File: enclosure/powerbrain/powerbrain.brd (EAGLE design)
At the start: 24.8 x 64.8 mm, 41 parts, among them Q2 200mA/50V, X2 ZX62D-B-5PA8

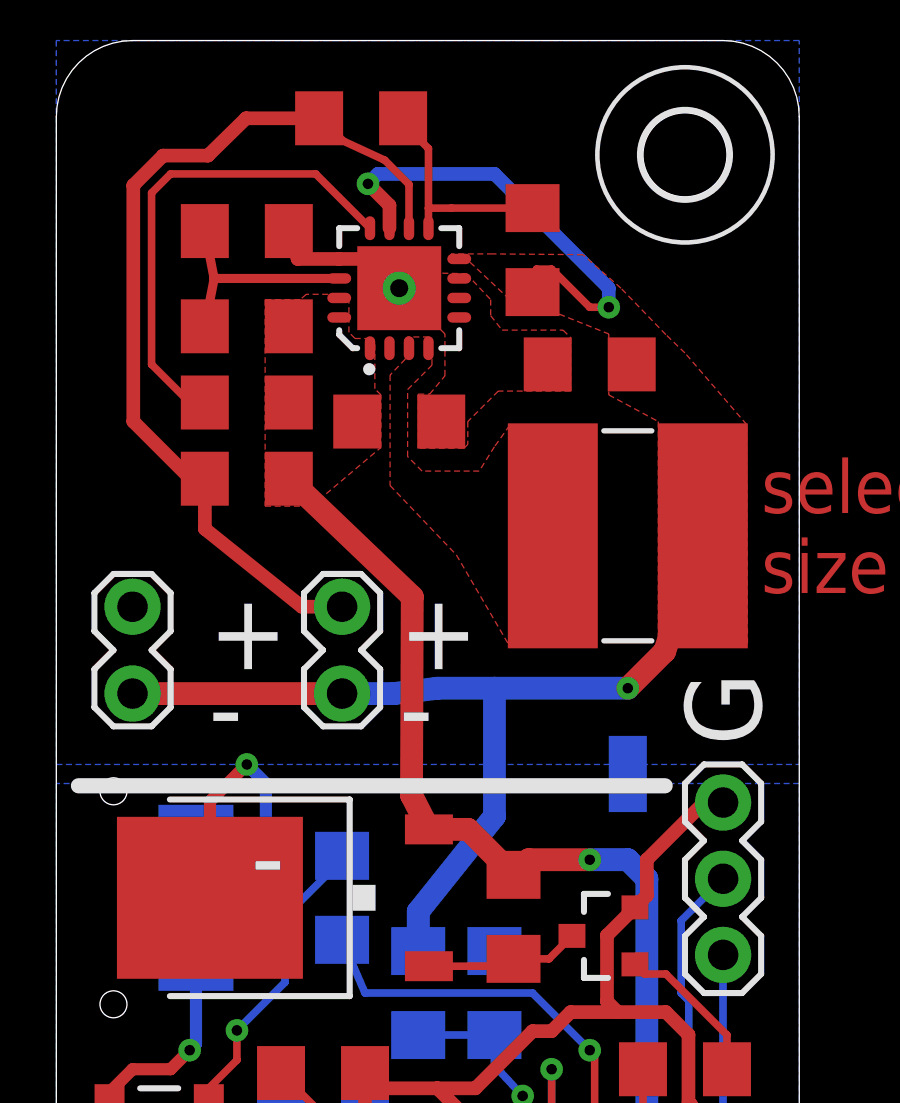
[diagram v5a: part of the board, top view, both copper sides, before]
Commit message: powerbrain: traces cleaned up
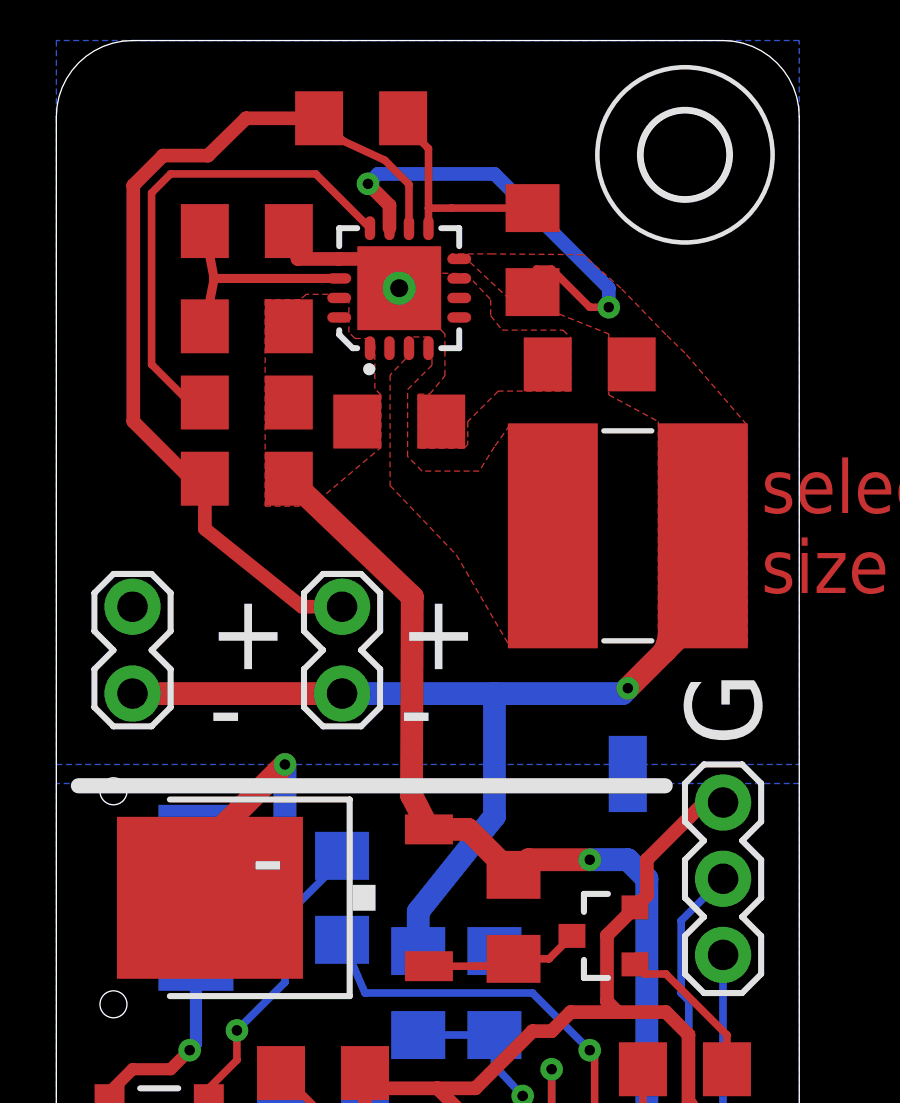
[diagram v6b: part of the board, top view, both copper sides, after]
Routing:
- net BATT_VCC: track 47.9 -> 49.6 mm
- net USB_VCC: track 11.6 -> 12.1 mm
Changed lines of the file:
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@@
 <vertex x="20.066" y="44.6786"/>
 </polygon>
-<wire x1="10.1854" y1="59.9948" x2="10.16" y2="59.9948" width="0.254" layer="1"/>
 <via x="10.3886" y="59.9948" extent="1-16" drill="0.35"/>
 <wire x1="12.065" y1="34.42" x2="12.065" y2="35.7378" width="0.762" layer="16"/>
-<wire x1="14.605" y1="38.9128" x2="12.065" y2="35.7378" width="0.762" layer="16"/>
+<wire x1="12.065" y1="35.7378" x2="14.605" y2="38.9128" width="0.762" layer="16"/>
 <via x="18.415" y="55.88" extent="1-16" drill="0.35"/>
 <wire x1="17.78" y1="55.88" x2="18.415" y2="55.88" width="0.254" layer="1"/>
@@
 <wire x1="16.51" y1="57.15" x2="16.005" y2="57.15" width="0.254" layer="1"/>
 <wire x1="16.005" y1="57.15" x2="15.875" y2="56.385" width="0.254" layer="1"/>
-<wire x1="9.525" y1="43.0022" x2="11.2522" y2="43.0022" width="0.762" layer="16"/>
-<wire x1="11.2522" y1="43.0022" x2="12.7" y2="43.18" width="0.762" layer="16"/>
-<wire x1="12.7" y1="43.18" x2="14.605" y2="43.18" width="0.762" layer="16"/>
-<wire x1="14.605" y1="43.18" x2="14.605" y2="38.9128" width="0.762" layer="16"/>
-<wire x1="14.605" y1="43.18" x2="19.05" y2="43.18" width="0.762" layer="16"/>
-<via x="19.05" y="43.18" extent="1-16" drill="0.35"/>
 <wire x1="21.55" y1="48.26" x2="20.28" y2="44.41" width="0.762" layer="1"/>
-<wire x1="20.28" y1="44.41" x2="19.05" y2="43.18" width="0.762" layer="1"/>
 <contactref element="J4" pad="2"/>
 <wire x1="2.54" y1="43.0022" x2="9.525" y2="43.0022" width="0.762" layer="1"/>
@@
 <wire x1="14.605" y1="60.325" x2="10.7188" y2="60.325" width="0.4572" layer="16"/>
 <wire x1="10.7188" y1="60.325" x2="10.3886" y2="59.9948" width="0.4572" layer="16"/>
-<wire x1="10.3886" y1="59.9948" x2="10.1854" y2="59.9948" width="0" layer="19" extent="1-1"/>
+<wire x1="14.605" y1="43.0022" x2="9.525" y2="43.0022" width="0.762" layer="16"/>
+<wire x1="14.605" y1="43.0022" x2="18.8722" y2="43.0022" width="0.762" layer="16"/>
+<wire x1="18.8722" y1="43.0022" x2="19.05" y2="43.18" width="0.762" layer="16"/>
+<via x="19.05" y="43.18" extent="1-16" drill="0.35"/>
+<wire x1="19.05" y1="43.18" x2="21.59" y2="45.72" width="0.762" layer="1"/>
+<wire x1="14.605" y1="38.9128" x2="14.605" y2="43.0022" width="0.762" layer="16"/>
 </signal>
 <signal name="N$4">
@@
 <signal name="USB_VCC">
 <contactref element="Q1" pad="3"/>
-<wire x1="5.12" y1="36.195" x2="5.12" y2="39.41" width="0.4064" layer="1"/>
-<wire x1="5.12" y1="39.41" x2="6.35" y2="40.64" width="0.4064" layer="1"/>
-<via x="6.35" y="40.64" extent="1-16" drill="0.35"/>
 <contactref element="S2" pad="2"/>
-<wire x1="4.655" y1="36.195" x2="6.35" y2="36.195" width="0.4064" layer="16"/>
-<wire x1="6.35" y1="36.195" x2="6.985" y2="36.83" width="0.4064" layer="16"/>
-<wire x1="6.985" y1="36.83" x2="6.985" y2="40.005" width="0.4064" layer="16"/>
-<wire x1="6.985" y1="40.005" x2="6.35" y2="40.64" width="0.4064" layer="16"/>
+<wire x1="5.12" y1="36.195" x2="5.12" y2="38.14" width="0.762" layer="1"/>
+<wire x1="5.12" y1="38.14" x2="7.62" y2="40.64" width="0.762" layer="1"/>
+<via x="7.62" y="40.64" extent="1-16" drill="0.35"/>
+<wire x1="7.62" y1="40.64" x2="7.62" y2="37.465" width="0.762" layer="16"/>
+<wire x1="7.62" y1="37.465" x2="6.35" y2="36.195" width="0.762" layer="16"/>
+<wire x1="6.35" y1="36.195" x2="4.655" y2="36.195" width="0.762" layer="16"/>
 </signal>
 <signal name="FOO3">

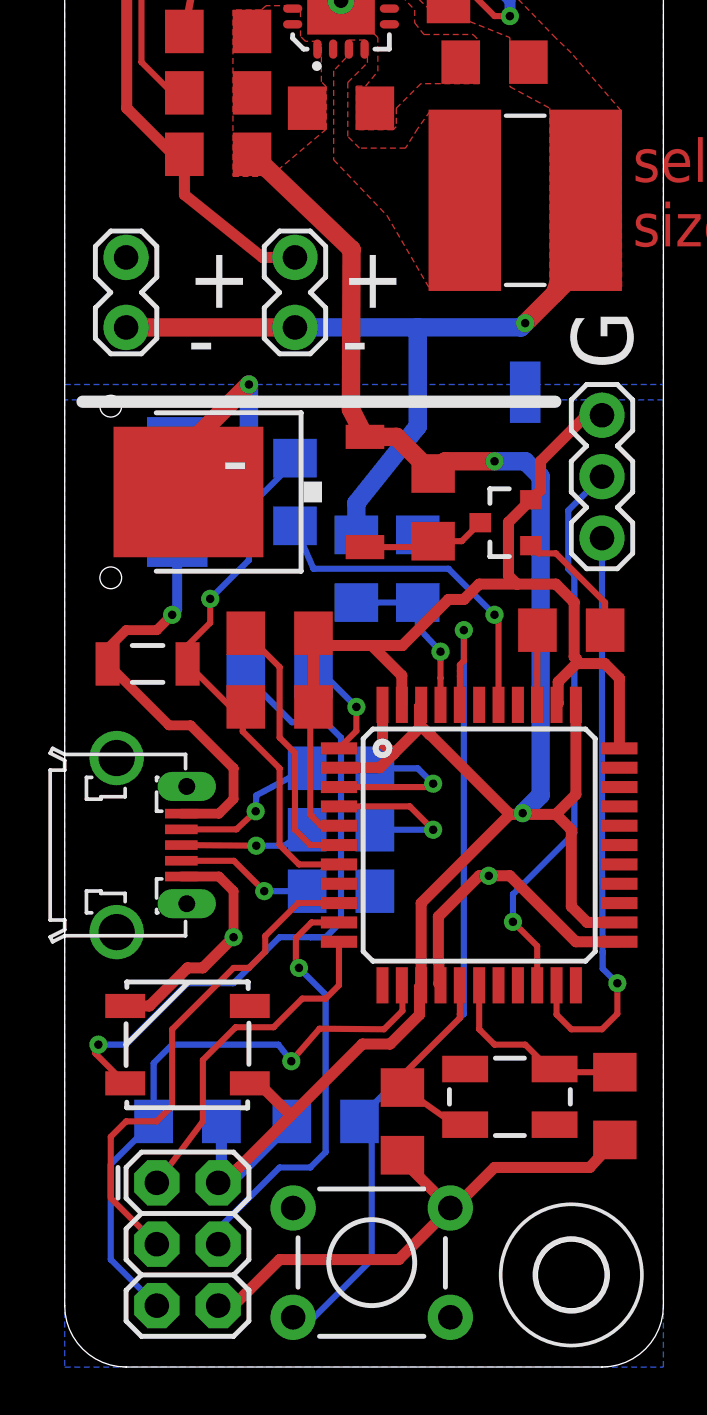
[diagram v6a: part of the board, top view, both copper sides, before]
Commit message: powerbrain: decoupling capacitor for battery voltage divider
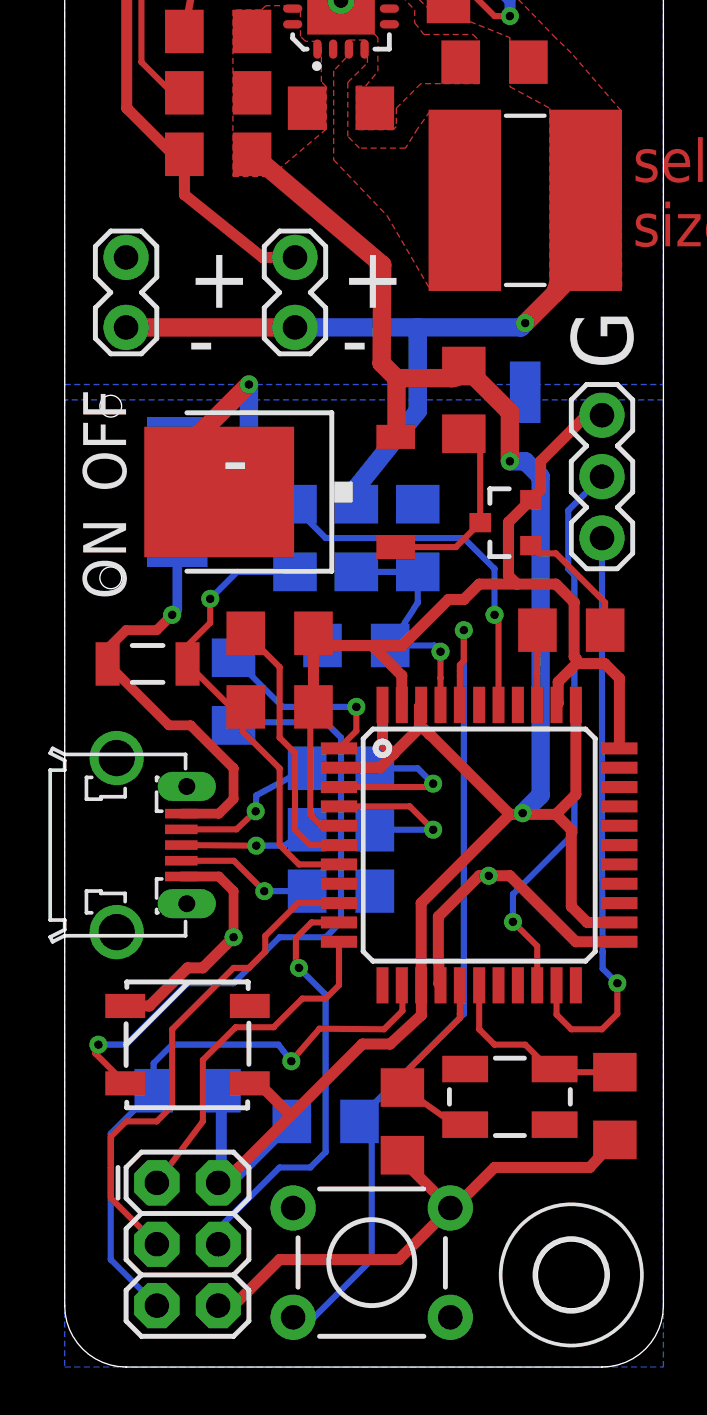
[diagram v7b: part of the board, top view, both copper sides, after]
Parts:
- added C1: 0.1uF, SparkFun-Passives:1206
- moved R3 4.62 mm to (16.5, 40.0)
- moved R_LED 2.01 mm to (6.99, 27.9), turned to 270 degrees
- moved RUSB3 1.91 mm to (9.53, 34.3), turned to 90 degrees
- moved Q1 1.27 mm to (8.89, 36.2)
- moved RRST 1.27 mm to (5.08, 11.4)
- moved VD1 1.27 mm to (12.1, 34.3)
- moved VD2 1.27 mm to (14.6, 34.3)
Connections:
- net GND: now also C1.2
- net VD_DIRECT: now also C1.1
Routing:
- net LED: track 4.31 -> 7.94 mm
- net $N23: track 22.7 -> 19.4 mm
- net VD_DIRECT: track 7.14 -> 10.3 mm
- net VCC: track 91.8 -> 94.9 mm
- net N$6: track 5.19 -> 7.88 mm
- net BATT_VCC: track 49.6 -> 48.3 mm
- net VBUS_SENSE: track 14.0 -> 15.1 mm
- net N$7: track 27.6 -> 26.7 mm
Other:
- board text added: "OFF"
- board text added: "ON"

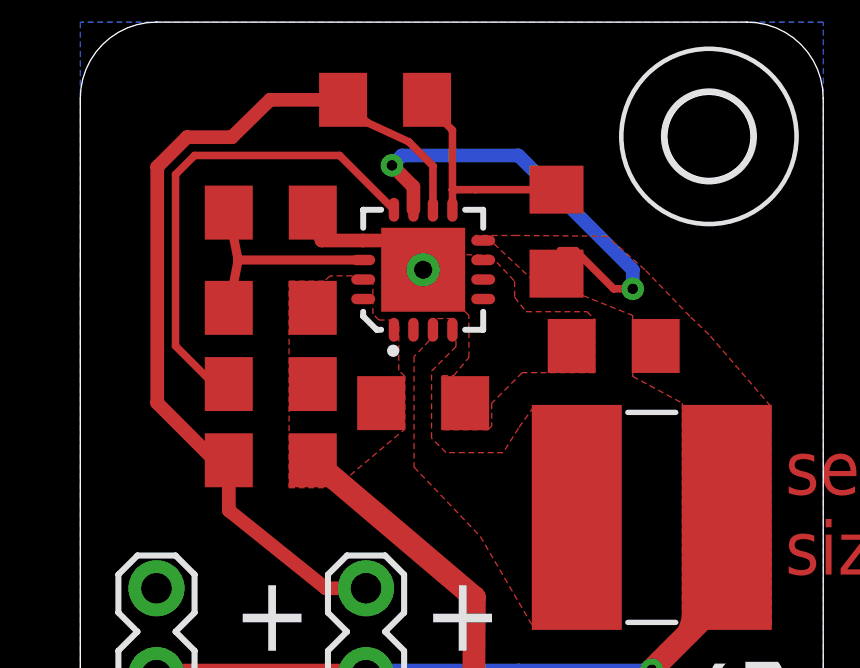
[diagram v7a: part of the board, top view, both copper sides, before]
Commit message: powerbrain: low battery output
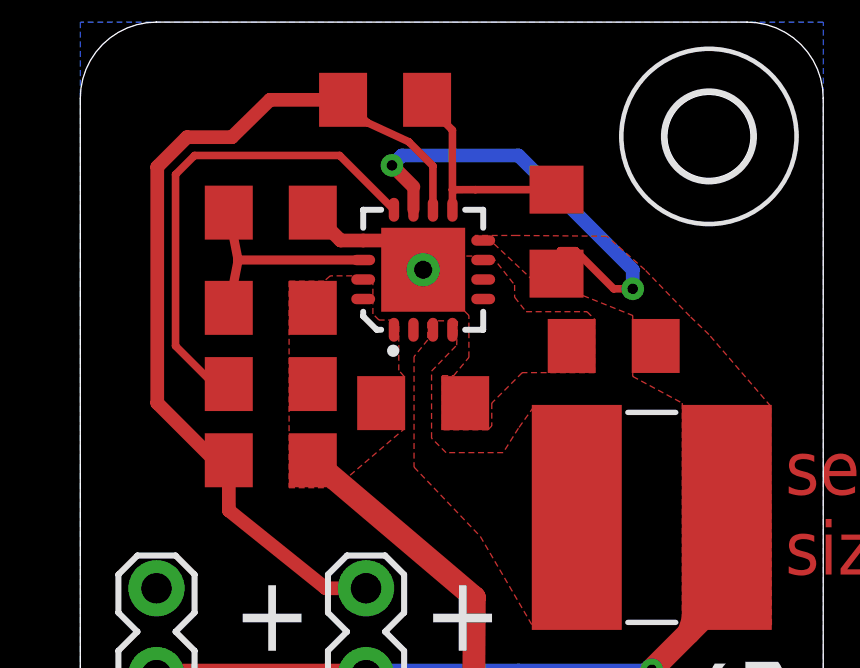
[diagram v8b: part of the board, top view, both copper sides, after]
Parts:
- BL1: value (none) -> 6.8uH / 2A
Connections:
- net N$16 renamed LOW_BATTERY_OUTPUT
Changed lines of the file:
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@@
 <?xml version="1.0" encoding="utf-8"?>
 <!DOCTYPE eagle SYSTEM "eagle.dtd">
-<eagle version="8.2.1">
+<eagle version="8.2.2">
 <drawing>
 <settings>
@@
 <attribute name="VALUE" x="6.35" y="46.99" size="1.27" layer="27" rot="R270"/>
 </element>
-<element name="BL1" library="SparkFun-Passives" package="NPI75C" value="" x="19.05" y="48.26" smashed="yes"/>
+<element name="BL1" library="SparkFun-Passives" package="NPI75C" value="6.8uH / 2A" x="19.05" y="48.26" smashed="yes"/>
 <element name="R3" library="SparkFun-Resistors" package="1206" value="10k" x="16.51" y="40.005" smashed="yes" rot="R270"/>
 <element name="R7" library="SparkFun-Resistors" package="1206" value="1k" x="20.955" y="30.48" smashed="yes"/>
@@
 <wire x1="13.208" y1="27.327" x2="13.145" y2="27.39" width="0.254" layer="1"/>
 <polygon width="0.0254" layer="1" thermals="no">
-<vertex x="10.8204" y="51.2064"/>
-<vertex x="10.8204" y="52.959"/>
+<vertex x="10.795" y="51.2064"/>
+<vertex x="10.795" y="52.959"/>
 <vertex x="10.6172" y="53.1622"/>
 <vertex x="10.6172" y="54.6862"/>
@@
 <contactref element="J4" pad="2"/>
 <wire x1="2.54" y1="43.0022" x2="9.525" y2="43.0022" width="0.762" layer="1"/>
-<wire x1="11.105" y1="58.515" x2="11.105" y2="59.2784" width="0.4572" layer="1"/>
+<wire x1="11.105" y1="58.515" x2="11.105" y2="59.2784" width="0.4064" layer="1"/>
 <wire x1="11.105" y1="59.2784" x2="10.3886" y2="59.9948" width="0.4572" layer="1"/>
 <wire x1="18.415" y1="55.88" x2="18.415" y2="56.515" width="0.4572" layer="16"/>
@@
 <wire x1="5.26" y1="56.825" x2="4.95" y2="55.245" width="0.3048" layer="1"/>
 </signal>
-<signal name="N$16">
+<signal name="LOW_BATTERY_OUTPUT">
 <contactref element="BR5" pad="2"/>
 <contactref element="U2" pad="12"/>
@@
 <vertex x="0" y="64.77"/>
 </polygon>
-<wire x1="8.045" y1="57.49" x2="9.43" y2="57.49" width="0.4572" layer="1"/>
-<wire x1="8.045" y1="57.49" x2="7.75" y2="58.42" width="0.4572" layer="1"/>
+<wire x1="8.68" y1="57.49" x2="9.43" y2="57.49" width="0.4572" layer="1"/>
+<wire x1="8.68" y1="57.49" x2="7.75" y2="58.42" width="0.4572" layer="1"/>
 <wire x1="9.43" y1="57.49" x2="10.455" y2="57.49" width="0.4572" layer="1"/>
 <wire x1="10.455" y1="57.49" x2="11.43" y2="56.515" width="0.4572" layer="1"/>
 <polygon width="0.127" layer="1" thermals="no">
-<vertex x="13.6652" y="56.9976"/>
-<vertex x="14.478" y="56.134"/>
+<vertex x="13.716" y="56.9722"/>
+<vertex x="14.478" y="56.007"/>
 <vertex x="14.478" y="55.6006"/>
 <vertex x="14.859" y="55.118"/>
@@
 <vertex x="12.446" y="55.499"/>
 <vertex x="12.446" y="56.896"/>
-<vertex x="12.5476" y="57.023"/>
+<vertex x="12.5476" y="56.9722"/>
 </polygon>
 <contactref element="U2" pad="10"/>
@@
 <vertex x="11.7094" y="50.9016"/>
 <vertex x="11.7094" y="53.1368"/>
-<vertex x="12.5222" y="53.9496"/>
-<vertex x="12.5222" y="54.7878"/>
-<vertex x="12.4206" y="54.8894"/>
-<vertex x="11.7094" y="54.8894"/>
-<vertex x="11.6332" y="54.8132"/>
-<vertex x="11.6332" y="54.1528"/>
+<vertex x="12.5476" y="54.0004"/>
+<vertex x="12.573" y="54.7878"/>
+<vertex x="12.446" y="54.8132"/>
+<vertex x="11.7094" y="54.8132"/>
+<vertex x="11.5824" y="54.7624"/>
+<vertex x="11.5824" y="54.1782"/>
 <vertex x="11.1252" y="53.6194"/>
 <vertex x="11.1252" y="49.9364"/>
